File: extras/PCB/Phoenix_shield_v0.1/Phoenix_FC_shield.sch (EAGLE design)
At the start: 51 parts, among them T1 BC817-40SMD, T2 BC817-40SMD

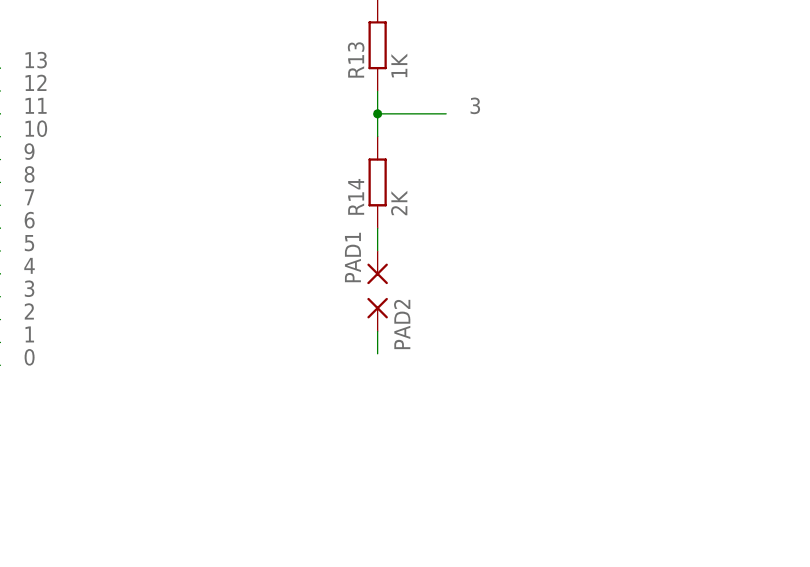
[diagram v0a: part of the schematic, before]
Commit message: PCB - tiny resistor value changes
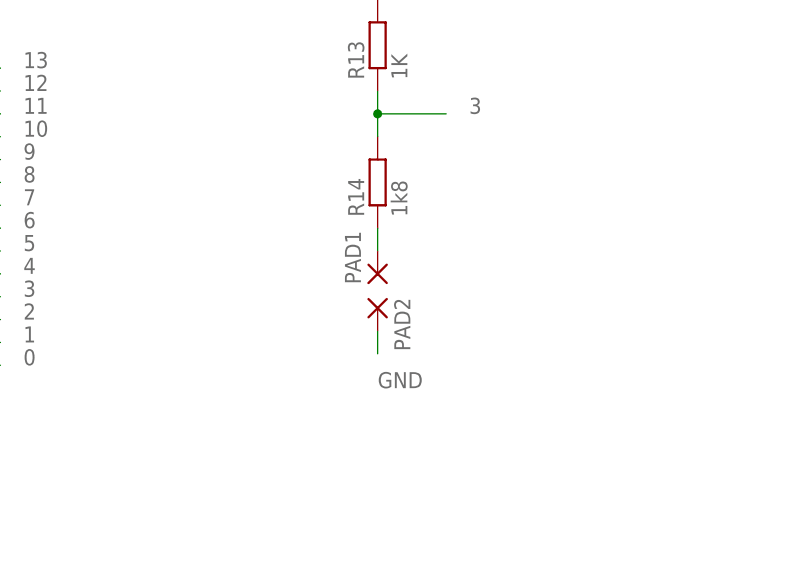
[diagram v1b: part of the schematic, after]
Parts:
- R14: value 2K -> 1k8
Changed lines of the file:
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@@
 <part name="D3" library="diode" deviceset="DIODE-" device="DO-214AC" value="1A"/>
 <part name="R13" library="resistor" deviceset="R-EU_" device="R0805" value="1K"/>
-<part name="R14" library="resistor" deviceset="R-EU_" device="R0805" value="2K"/>
+<part name="R14" library="resistor" deviceset="R-EU_" device="R0805" value="1k8"/>
 <part name="PAD1" library="wirepad" deviceset="WIREPAD" device="SMD1,27-254"/>
 <part name="PAD2" library="wirepad" deviceset="WIREPAD" device="SMD1,27-254"/>
@@
 <pinref part="PAD2" gate="G$1" pin="P"/>
 <wire x1="180.34" y1="-81.28" x2="180.34" y2="-83.82" width="0.1524" layer="91"/>
+<label x="180.34" y="-87.63" size="1.778" layer="95"/>
 </segment>
 </net>
